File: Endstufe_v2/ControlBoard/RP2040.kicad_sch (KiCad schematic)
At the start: 34 parts, among them J19 Conn_01x06_Pin, J8 DNP, J9 DNP, SW1 TS-1187A-B-A-B, SW2 TS-1187A-B-A-B, U4 TYPE-C 16PFS 2JCB1.2-H6.5 IPX8, U5 W25Q128JVS, U6 RP2040, Y1 12Mhz

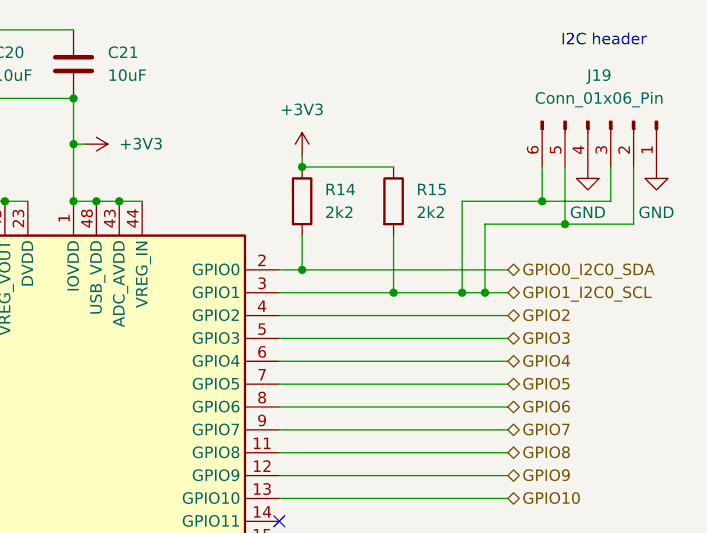
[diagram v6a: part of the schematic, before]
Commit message: Routed all connections of control board
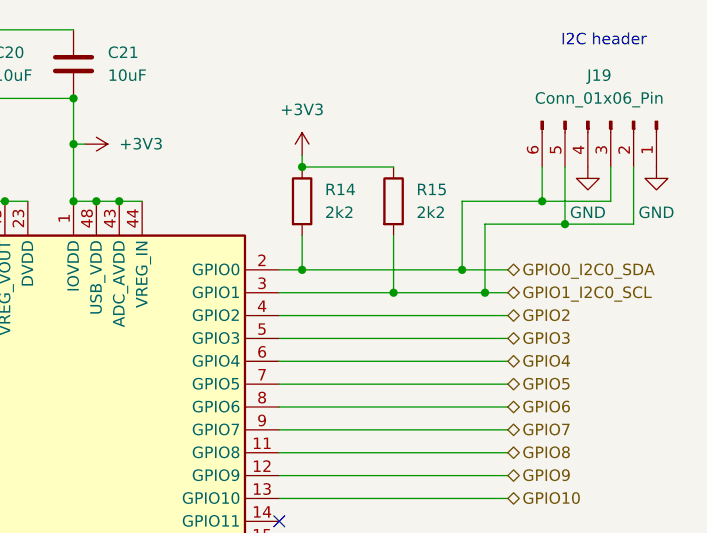
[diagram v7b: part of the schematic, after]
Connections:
- net GPIO0_I2C0_SDA: now also J19.3 (Pin_3), J19.6 (Pin_6)
- net GPIO1_I2C0_SCL: no longer J19.3 (Pin_3), J19.6 (Pin_6)
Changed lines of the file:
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@@
+	)
+	(junction
+		(at 246.38 53.34)
+		(diameter 0)
+		(color 0 0 0 0)
 	)
 	(junction
@@
 	)
 	(junction
+		(at 255.27 45.72)
+		(diameter 0)
+		(color 0 0 0 0)
+	)
+	(junction
 		(at 45.72 140.97)
 		(diameter 0)
@@
 	)
 	(junction
-		(at 255.27 45.72)
-		(diameter 0)
-		(color 0 0 0 0)
-	)
-	(junction
 		(at 248.92 55.88)
 		(diameter 0)
@@
 	(junction
 		(at 238.76 55.88)
-		(diameter 0)
-		(color 0 0 0 0)
-	)
-	(junction
-		(at 246.38 55.88)
 		(diameter 0)
 		(color 0 0 0 0)
@@
 	(wire
 		(pts
-			(xy 246.38 45.72) (xy 246.38 55.88)
+			(xy 246.38 45.72) (xy 246.38 53.34)
 		)
 		(stroke
@@
 	(wire
 		(pts
-			(xy 246.38 55.88) (xy 248.92 55.88)
+			(xy 238.76 55.88) (xy 248.92 55.88)
 		)
 		(stroke
@@
 	(wire
 		(pts
-			(xy 238.76 55.88) (xy 246.38 55.88)
-		)
-		(stroke
-			(width 0)
-			(type default)
-		)
-	)
-	(wire
-		(pts
 			(xy 45.72 163.83) (xy 76.2 163.83)
 		)
@@
 	(wire
 		(pts
+			(xy 255.27 41.91) (xy 255.27 45.72)
+		)
+		(stroke
+			(width 0)
+			(type default)
+		)
+	)
+	(wire
+		(pts
 			(xy 101.6 26.67) (xy 114.3 26.67)
 		)
@@
 	(wire
 		(pts
+			(xy 246.38 53.34) (xy 228.6 53.34)
+		)
+		(stroke
+			(width 0)
+			(type default)
+		)
+	)
+	(wire
+		(pts
 			(xy 248.92 48.26) (xy 248.92 55.88)
 		)
@@
 	(wire
 		(pts
-			(xy 251.46 53.34) (xy 228.6 53.34)
+			(xy 251.46 53.34) (xy 246.38 53.34)
 		)
 		(stroke
@@
 		)
 		(stroke
-			(width 0)
-			(type default)
-		)
-	)
-	(wire
-		(pts
-			(xy 255.27 41.91) (xy 255.27 45.72)
-		)
-		(stroke

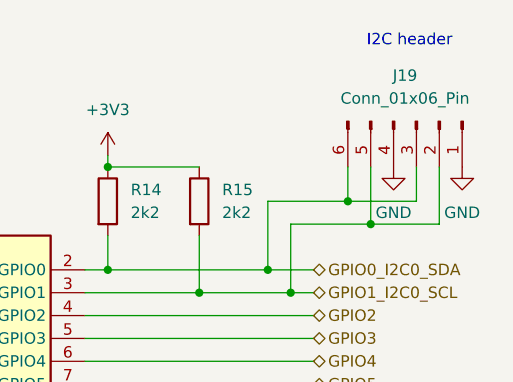
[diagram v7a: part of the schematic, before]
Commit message: Change unavailable parts to available ones, optimise silkscreen, do via stiching
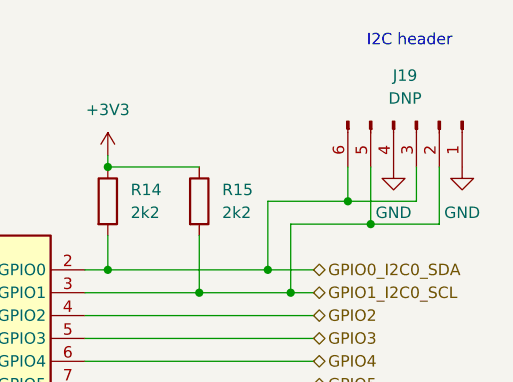
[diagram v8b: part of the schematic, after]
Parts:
- C10, C11: footprint Endstufe:C_0603_1608Metric -> Endstufe:C_0402_1005Metric; LCSC Part # C1658 -> C526980
- J19: value Conn_01x06_Pin -> DNP; footprint Connector_PinHeader_2.54mm:PinHeader_1x06_P2.54mm_Vertical -> Endstufe:PinHeader_1x06_P2.54mm_Vertical
- J8: footprint Connector_PinHeader_2.54mm:PinHeader_1x05_P2.54mm_Vertical -> Endstufe:PinHeader_1x05_P2.54mm_Vertical
- R14, R15: footprint Resistor_SMD:R_0805_2012Metric_Pad1.20x1.40mm_HandSolder -> Endstufe:R_0805_2012Metric_Pad1.20x1.40mm_HandSolder
- TP2: footprint TestPoint:TestPoint_Pad_D1.0mm -> Endstufe:TestPoint_Pad_D1.0mm
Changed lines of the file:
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@@
 			)
 		)
-		(property "Footprint" "Endstufe:C_0603_1608Metric"
+		(property "Footprint" "Endstufe:C_0402_1005Metric"
 			(at 129.54 108.2548 0)
 			(effects
@@
 			)
 		)
-		(property "LCSC Part #" "C1658"
+		(property "LCSC Part #" "C526980"
 			(at 125.73 109.22 0)
 			(effects
@@
 			)
 		)
-		(property "Footprint" "Resistor_SMD:R_0805_2012Metric_Pad1.20x1.40mm_HandSolder"
+		(property "Footprint" "Endstufe:R_0805_2012Metric_Pad1.20x1.40mm_HandSolder"
 			(at 236.982 45.72 90)
 			(effects
@@
 			)
 		)
-		(property "Value" "Conn_01x06_Pin"
+		(property "Value" "DNP"
 			(at 261.62 34.29 90)
 			(effects
@@
 			)
 		)
-		(property "Footprint" "Connector_PinHeader_2.54mm:PinHeader_1x06_P2.54mm_Vertical"
+		(property "Footprint" "Endstufe:PinHeader_1x06_P2.54mm_Vertical"
 			(at 262.89 36.83 0)
 			(effects
@@
 			)
 		)
-		(property "Footprint" "TestPoint:TestPoint_Pad_D1.0mm"
+		(property "Footprint" "Endstufe:TestPoint_Pad_D1.0mm"
 			(at 111.76 53.34 0)
 			(effects
@@
 			)
 		)
-		(property "Footprint" "Endstufe:C_0603_1608Metric"
+		(property "Footprint" "Endstufe:C_0402_1005Metric"
 			(at 129.54 98.0948 0)
 			(effects
@@
 			)
 		)
-		(property "LCSC Part #" "C1658"
+		(property "LCSC Part #" "C526980"
 			(at 125.73 99.06 0)
 			(effects
@@
 			)
 		)
-		(property "Footprint" "Connector_PinHeader_2.54mm:PinHeader_1x05_P2.54mm_Vertical"
+		(property "Footprint" "Endstufe:PinHeader_1x05_P2.54mm_Vertical"
 			(at 134.62 132.08 0)
 			(effects
@@
 			)
 		)
-		(property "Footprint" "Resistor_SMD:R_0805_2012Metric_Pad1.20x1.40mm_HandSolder"
+		(property "Footprint" "Endstufe:R_0805_2012Metric_Pad1.20x1.40mm_HandSolder"
 			(at 226.822 45.72 90)
 			(effects
